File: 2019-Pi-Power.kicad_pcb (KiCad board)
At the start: 2 copper layers, 65 x 56 mm, 37 parts, among them J1 Barrel_Jack_Switch, J2 Conn_01x04, J3 Conn_01x04, J4 Conn_02x04_Odd_Even, J5 Conn_01x04, J6 Conn_01x04, J7 Conn_02x02_Odd_Even, P1 Conn_02x20_Odd_Even, U1 MP1584, U2 MP1584

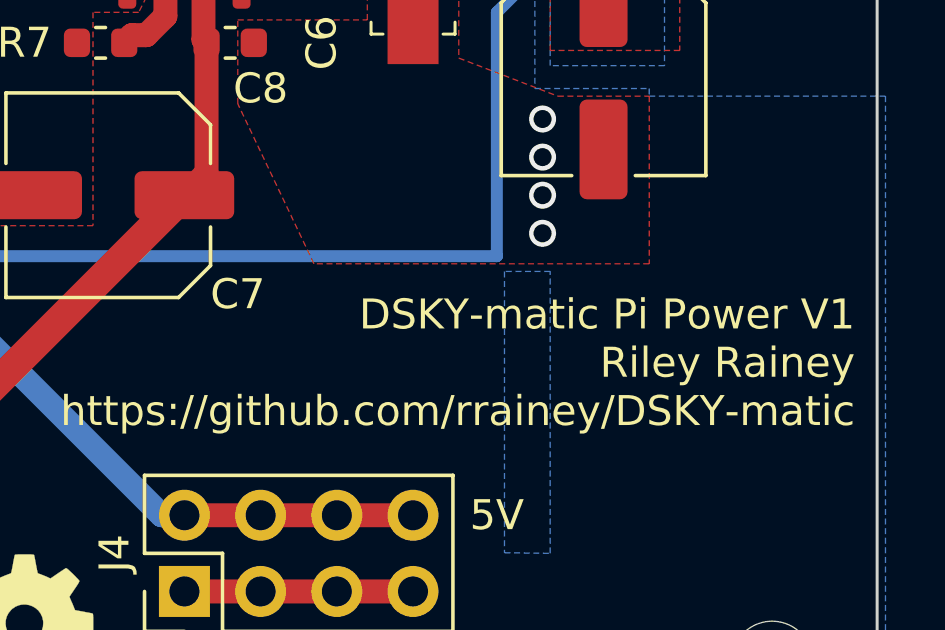
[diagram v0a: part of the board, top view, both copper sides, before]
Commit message: V2 board: fix issue with + power input on back of board
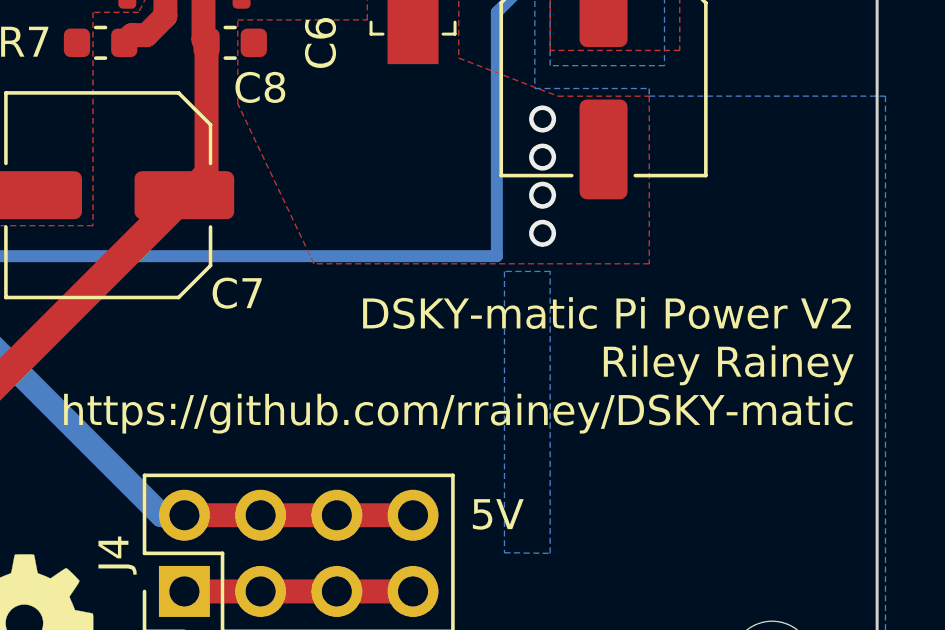
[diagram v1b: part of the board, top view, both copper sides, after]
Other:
- board text added: "DSKY-matic Pi Power V2 Riley Rainey https://github.com/rrainey/DSKY-matic"
- board text removed: "DSKY-matic Pi Power V1 Riley Rainey https://github.com/rrainey/DSKY-matic"

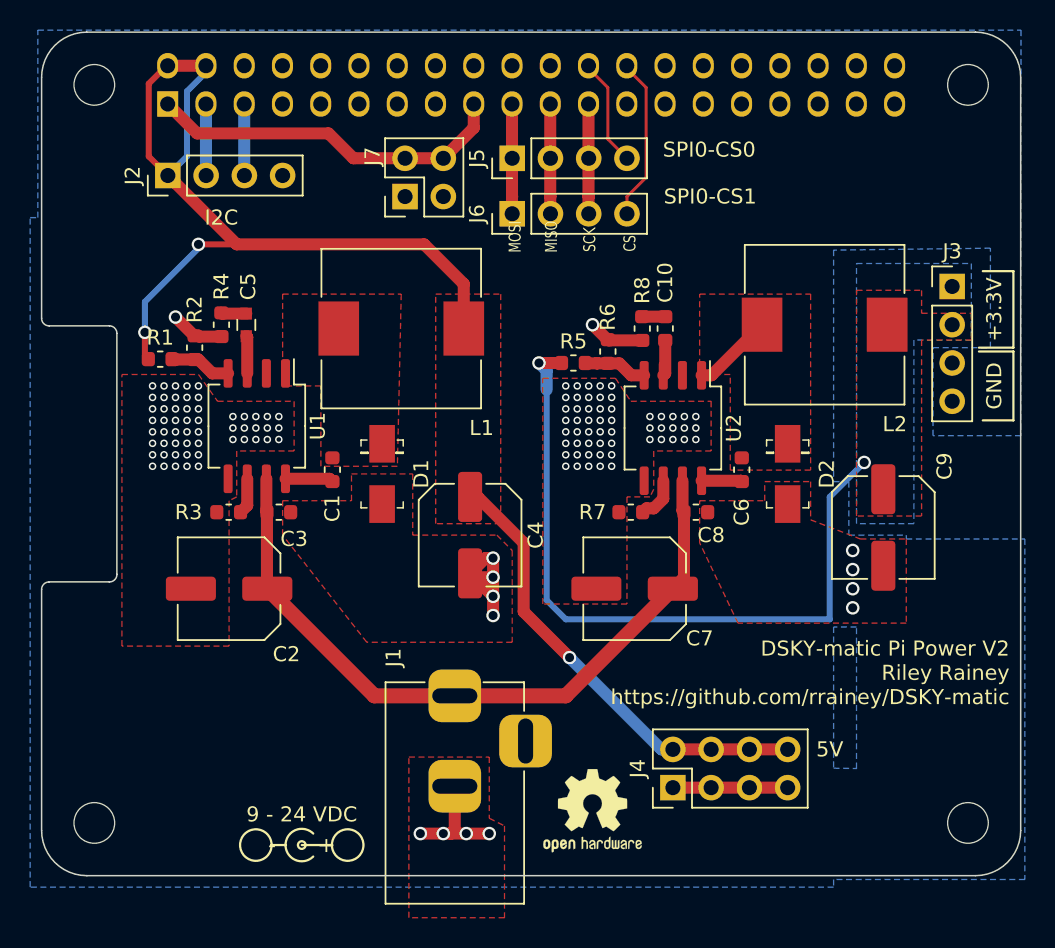
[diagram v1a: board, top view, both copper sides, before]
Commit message: V3 Board - adds Molex I2C interconnect
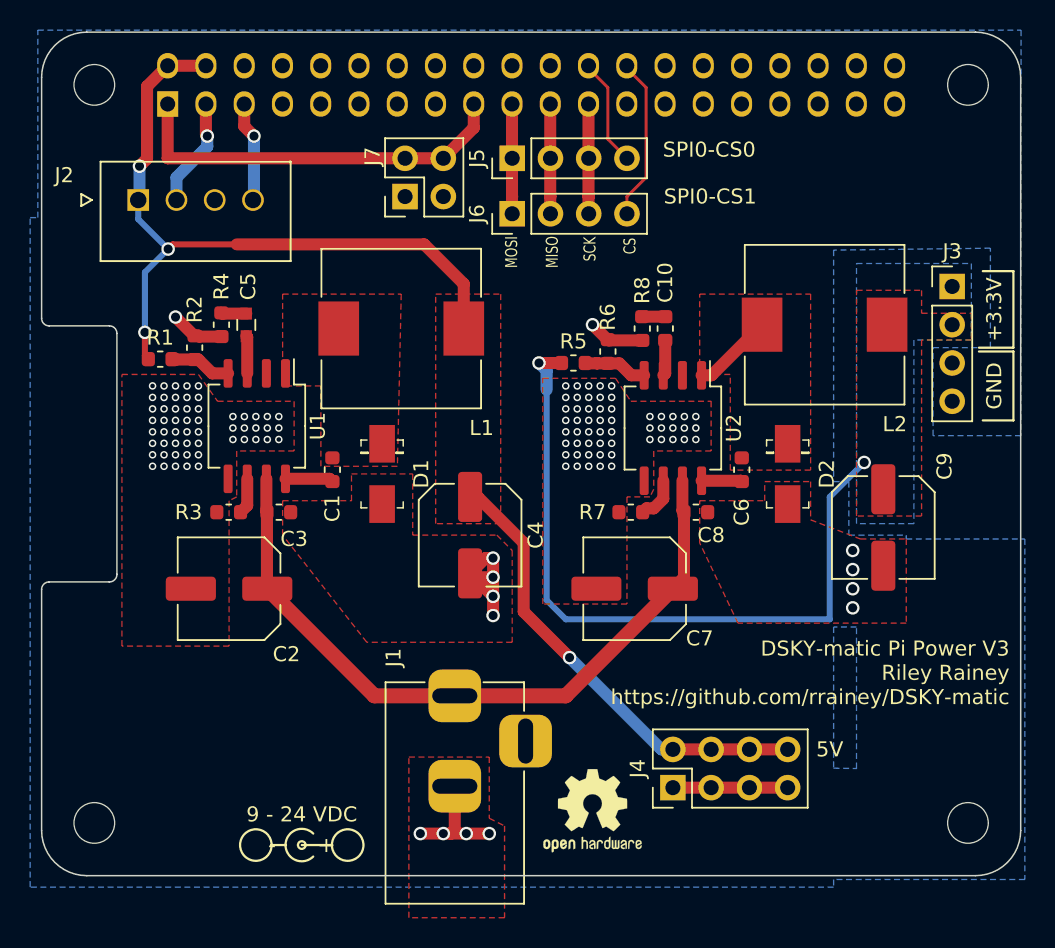
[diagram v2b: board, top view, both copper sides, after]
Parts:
- J2: value Conn_01x04 -> 1719710004; footprint Connector_PinHeader_2.54mm:PinHeader_1x04_P2.54mm_Vertical -> Pi-Power:MOLEX_1719710004
- moved J2 2.55 mm to (206.4, 105.1), turned to 180 degrees
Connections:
- J1 pad 3: (no net) -> unconnected-(J1-Pad3)
- J2 pad 3: /GPIO3(SCL1) -> GND
- J2 pad 4: GND -> /GPIO3(SCL1)
- P1 pad 10: (no net) -> /GPIO15(RXD0)
- P1 pad 11: (no net) -> /GPIO17(GEN0)
- P1 pad 12: (no net) -> /GPIO18(GEN1)(PWM0)
- P1 pad 13: (no net) -> /GPIO27(GEN2)
- P1 pad 15: (no net) -> /GPIO22(GEN3)
- P1 pad 16: (no net) -> /GPIO23(GEN4)
- P1 pad 18: (no net) -> /GPIO24(GEN5)
- P1 pad 22: (no net) -> /GPIO25(GEN6)
- P1 pad 27: (no net) -> /ID_SD
- P1 pad 28: (no net) -> /ID_SC
- P1 pad 29: (no net) -> /GPIO5
- P1 pad 31: (no net) -> /GPIO6
- P1 pad 32: (no net) -> /GPIO12(PWM0)
- P1 pad 33: (no net) -> /GPIO13(PWM1)
- P1 pad 35: (no net) -> /GPIO19(SPI1_MISO)
- P1 pad 36: (no net) -> /GPIO16
- P1 pad 37: (no net) -> /GPIO26
- P1 pad 38: (no net) -> /GPIO20(SPI1_MOSI)
- P1 pad 40: (no net) -> /GPIO21(SPI1_SCK)
- P1 pad 7: (no net) -> /GPIO4(GCLK)
- P1 pad 8: (no net) -> /GPIO14(TXD0)
- U1 pad 2: (no net) -> unconnected-(U1-Pad2)
- U2 pad 2: (no net) -> unconnected-(U2-Pad2)
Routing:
- net +5V: track 87.3 -> 79.4 mm, vias 3 -> 4
- net /GPIO2(SDA1): track 4.75 -> 7.26 mm, vias 0 -> 1
- net +3V3: track 24.2 -> 26.3 mm
- net /GPIO3(SCL1): track 4.75 -> 6.67 mm, vias 0 -> 1
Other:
- net class Default removed
- net class Power removed
- board text added: "DSKY-matic Pi Power V3 Riley Rainey https://github.com/rrainey/DSKY-matic"
- board text removed: "DSKY-matic Pi Power V2 Riley Rainey https://github.com/rrainey/DSKY-matic"
- board text removed: "I2C"

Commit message: V4 PCB
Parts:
- C5: footprint Capacitors_SMD:C_0603 -> Capacitor_SMD:C_0603_1608Metric
- J5, J6: footprint Pin_Headers:Pin_Header_Straight_1x04_Pitch2.54mm -> Connector_PinHeader_2.54mm:PinHeader_1x04_P2.54mm_Vertical
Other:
- board text added: "DSKY-matic Pi Power V4 Riley Rainey https://github.com/rrainey/Pi-Power"
- board text removed: "DSKY-matic Pi Power V3 Riley Rainey https://github.com/rrainey/DSKY-matic"
